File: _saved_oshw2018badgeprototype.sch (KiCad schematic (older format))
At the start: 72 parts, among them J1 Conn_02x03_Top_Bottom, J2 105162-0001, Q2 Q_NMOS_GSD, SW1 SW_Push, T1 TEST_1P, T2 TEST_1P, T3 TEST_1P, T4 TEST_1P, T5 TEST_1P, T6 TEST_1P, U1 ESP32-WROOM, U10 WS2812B, U11 WS2812B, U12 WS2812B, U13 WS2812B, U14 WS2812B, U15 WS2812B, U16 WS2812B, U17 WS2812B, U18 WS2812B, U19 WS2812B, U2 XC9141, U20 WS2812B, U3 KX122-1037, U4 Si7006-A20, U5 WS2812B, U6 WS2812B, U7 WS2812B, U8 WS2812B, U9 WS2812B, X1 52435-2471, X2 Badgelife_shitty_connector

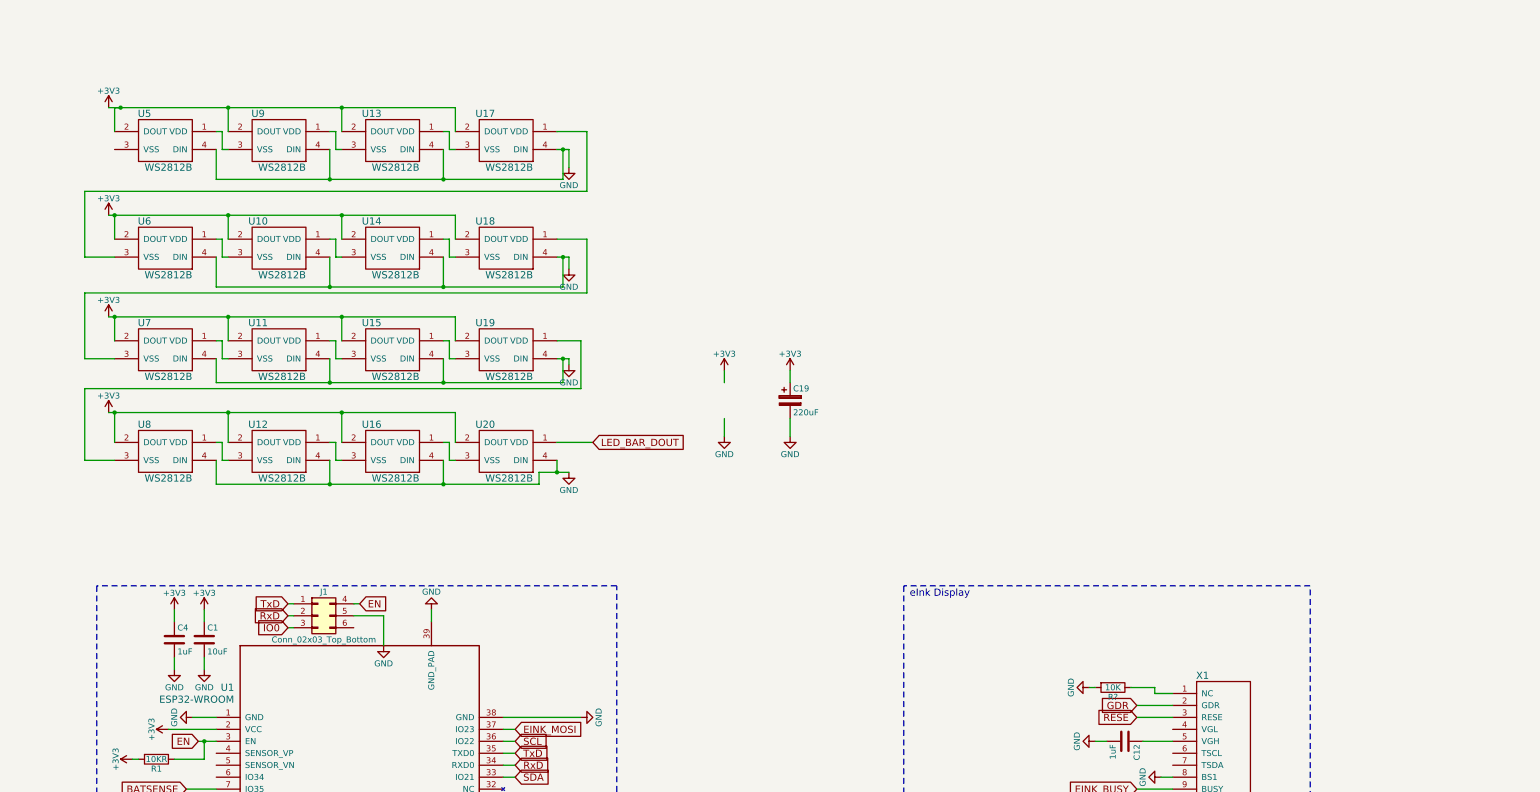
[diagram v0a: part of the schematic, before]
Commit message: fixed LEDs
Fixed LED footprint, fixed traces, reduced LEDs to 6
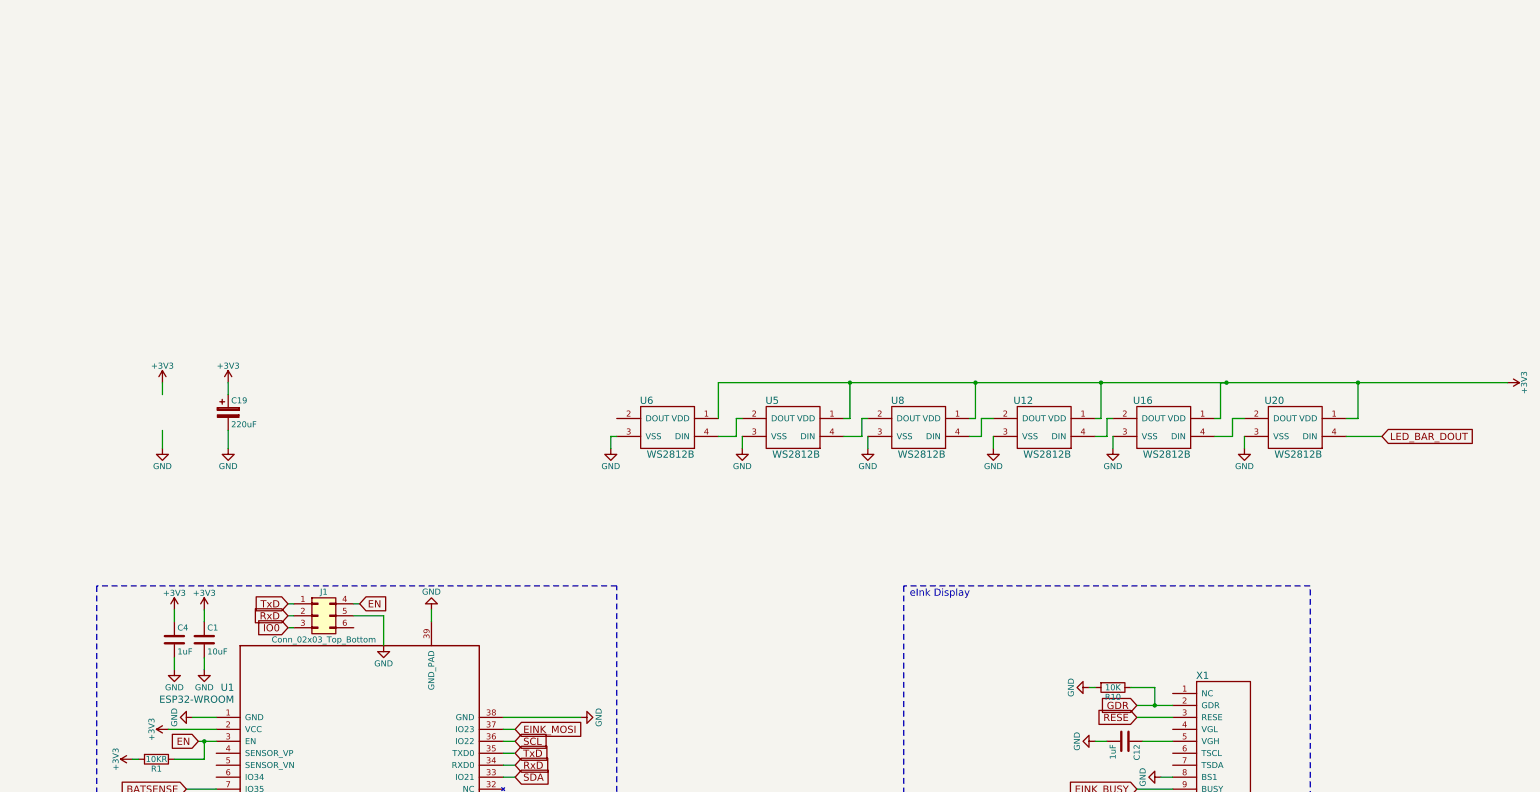
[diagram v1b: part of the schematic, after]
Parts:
- removed U10, U11, U13, U14, U15, U17, U18, U19, U7, U9: WS2812B, WS2812B:ws2812B_mini, symbol WS2812B
- gave numbers to parts that had none: 1
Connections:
- wire segments 329 -> 263
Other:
- moved on the sheet: C19, U12, U16, U20, U8
